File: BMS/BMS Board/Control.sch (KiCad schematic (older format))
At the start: 12 parts, among them J2 640456-3, M22 AO3402, Q2 AO3402, U29 MCP23008-E_SO, U30 MCP23008-E_SO, U31 MCP23008-E_SO

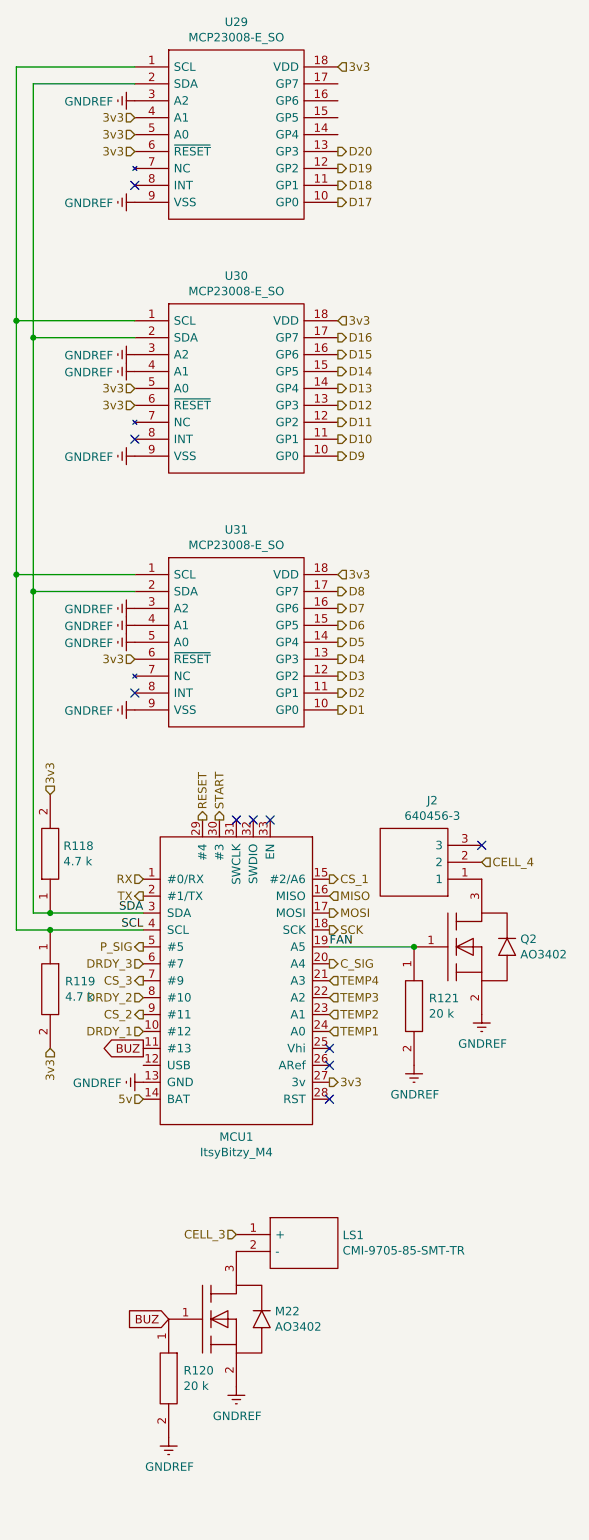
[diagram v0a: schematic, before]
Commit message: "SingleDigitNumberSelector" now blinks when idle.
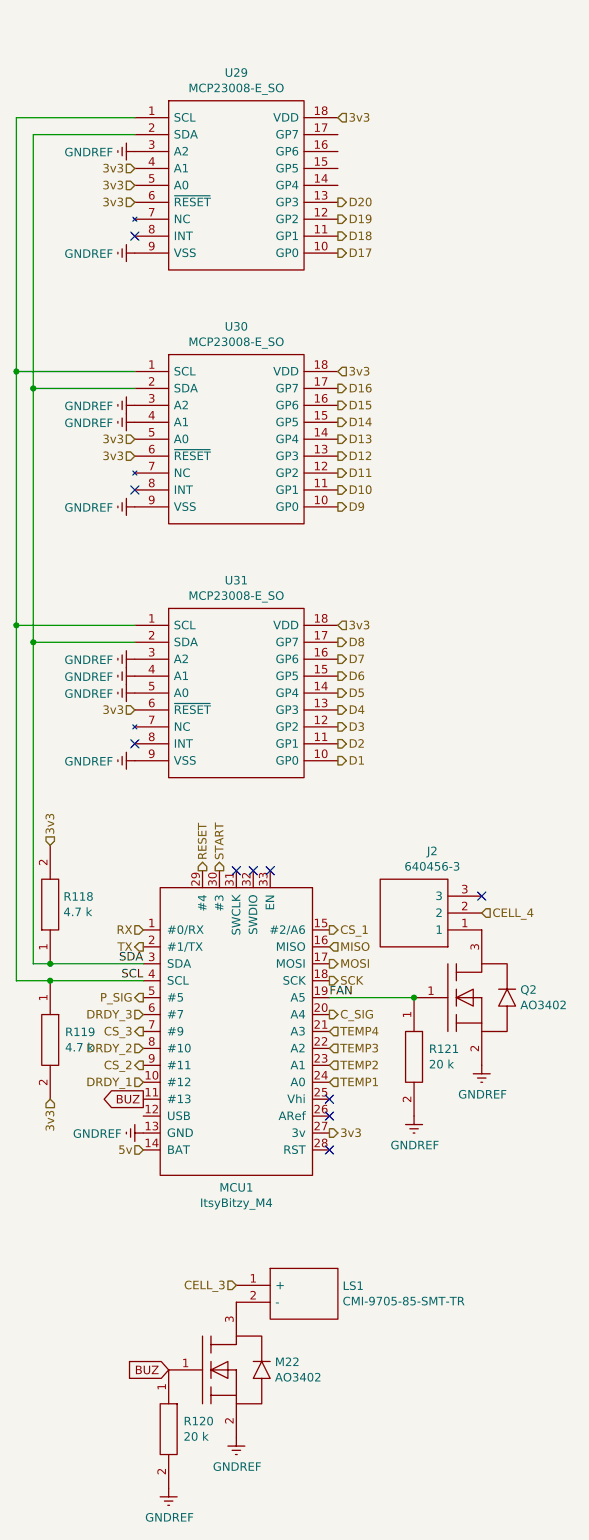
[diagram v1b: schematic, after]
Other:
- moved on the sheet: J2, LS1, M22, MCU1, Q2, R118, R119, R120, R121, U29, U30, U31

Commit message: ...
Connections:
- net 3v3: no longer U29.5 (A0)
- net GNDREF: now also U29.5 (A0)
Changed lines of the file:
@@
 	0    1    1    0
 $EndComp
-Text HLabel 3650 1550 0    50   Input ~ 0
-3v3
 $Comp
 L power:GNDREF #PWR0140
@@
 	1    0    0    -1
 $EndComp
+$Comp
+L power:GNDREF #PWR0154
+U 1 1 5EF1F064
+P 3650 1550
+F 0 "#PWR0154" H 3650 1300 50  0001 C CNN
+F 1 "GNDREF" V 3655 1422 50  0000 R CNN
+F 2 "" H 3650 1550 50  0001 C CNN
+F 3 "" H 3650 1550 50  0001 C CNN
+	1    3650 1550
+	0    1    1    0
+$EndComp
 $EndSCHEMATC

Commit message: workin on BMS also reset my computer so KiCad added some recovery files
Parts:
- M22, Q2: symbol MOSFET:AO3402 -> BMS-Board-rescue:AO3402-MOSFET
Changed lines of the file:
@@
 $EndComp
 $Comp
-L MOSFET:AO3402 M?
+L BMS-Board-rescue:AO3402-MOSFET M?
 U 1 1 5EE20212
 P 4250 8550
 AR Path="/5E8E2BA1/5EE20212" Ref="M?"  Part="1"
 AR Path="/5E8E2E94/5EE20212" Ref="M22"  Part="1"
+AR Path="/5EE20212" Ref="M22"  Part="1"
 F 0 "M22" H 4478 8596 50  0000 L CNN
 F 1 "AO3402" H 4478 8505 50  0000 L CNN
@@
 $EndComp
 $Comp
-L MOSFET:AO3402 Q2
+L BMS-Board-rescue:AO3402-MOSFET Q2
 U 1 1 5F09000B
 P 5700 6350
